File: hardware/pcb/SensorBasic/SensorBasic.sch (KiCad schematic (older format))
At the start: 4 parts

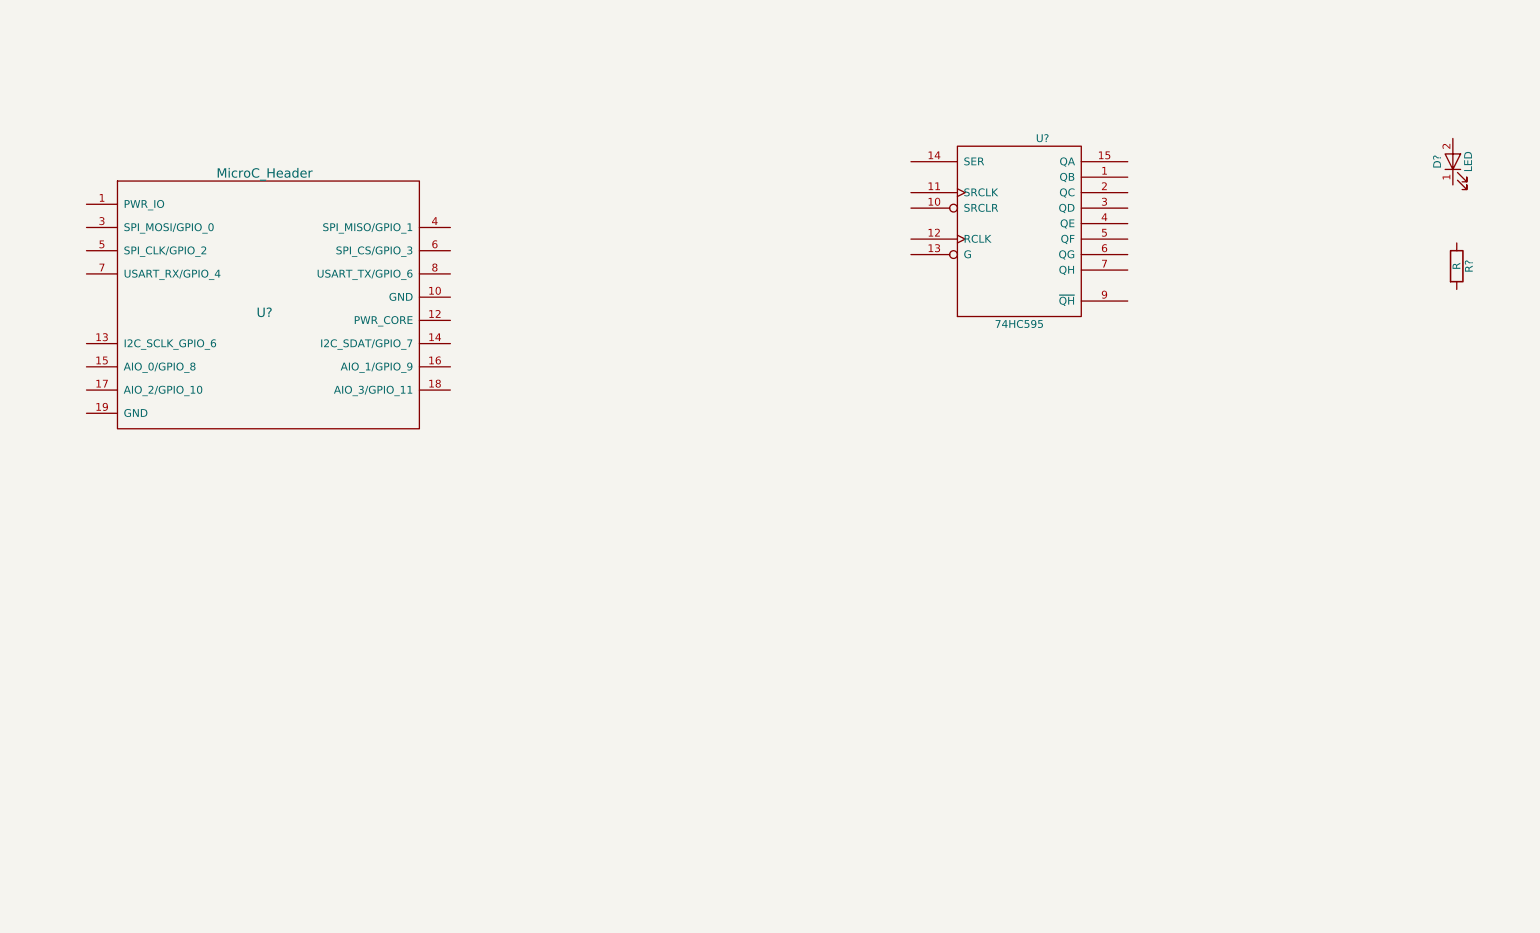
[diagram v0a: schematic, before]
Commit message: Initial schematic for Sensor
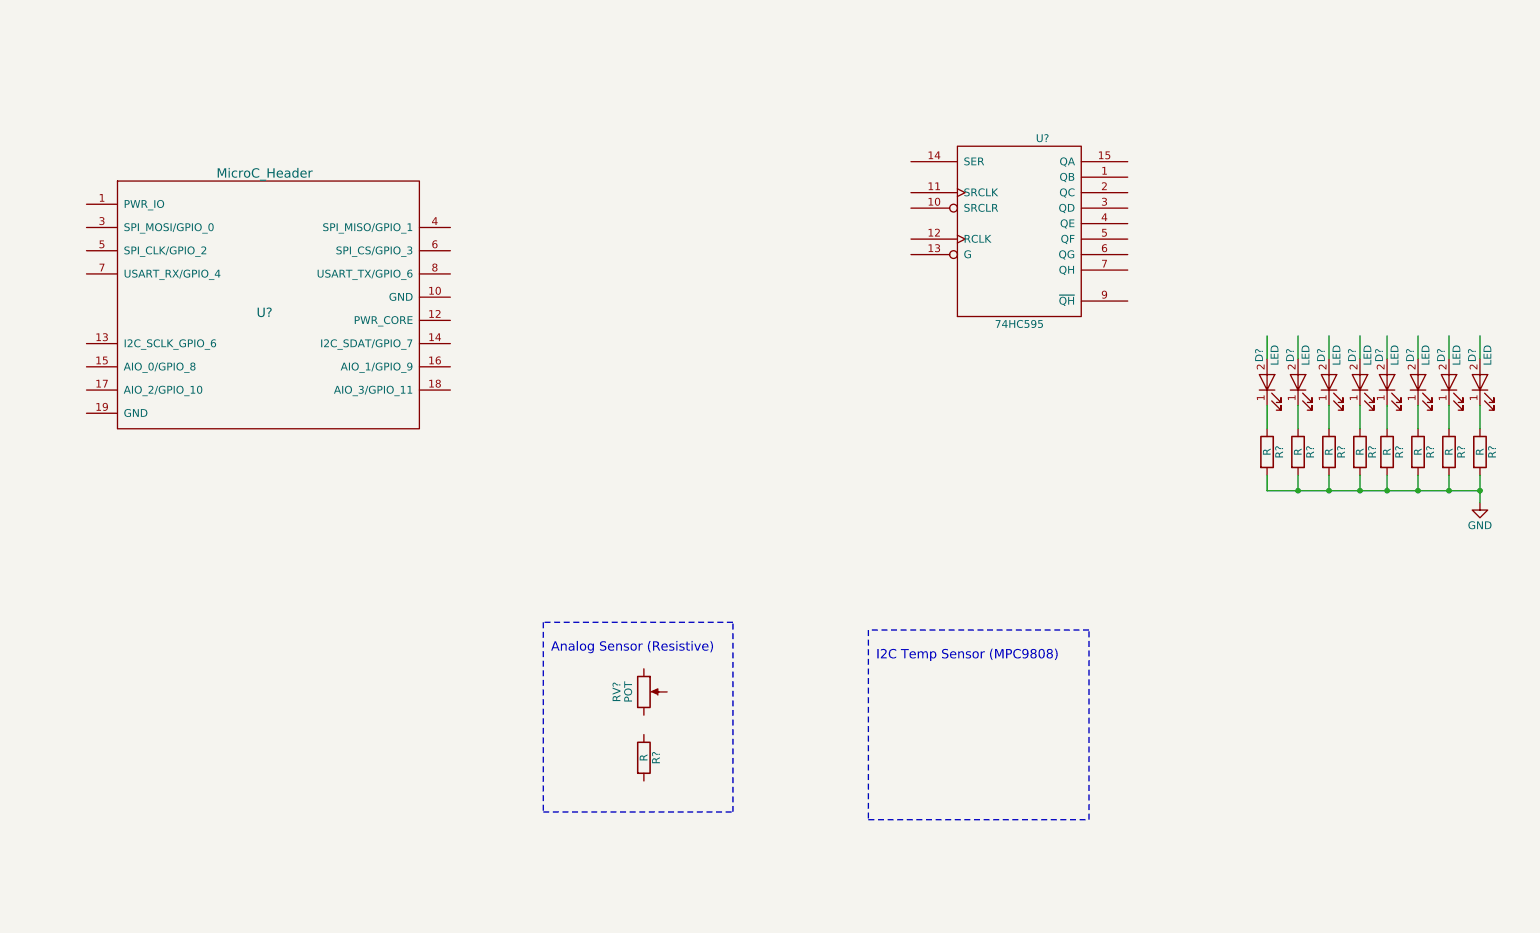
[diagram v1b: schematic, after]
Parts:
- added D? (x7): LED, symbol LED
- added R? (x8): R, symbol R
- added RV?: POT, symbol POT
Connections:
- net labels added: GND
- wire segments 0 -> 32
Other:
- note added: "Analog Sensor (Resistive)"
- note added: "I2C Temp Sensor (MPC9808)"
- moved on the sheet: D?, R?

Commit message: Add schematics symbol for temperature sensor, DS7505
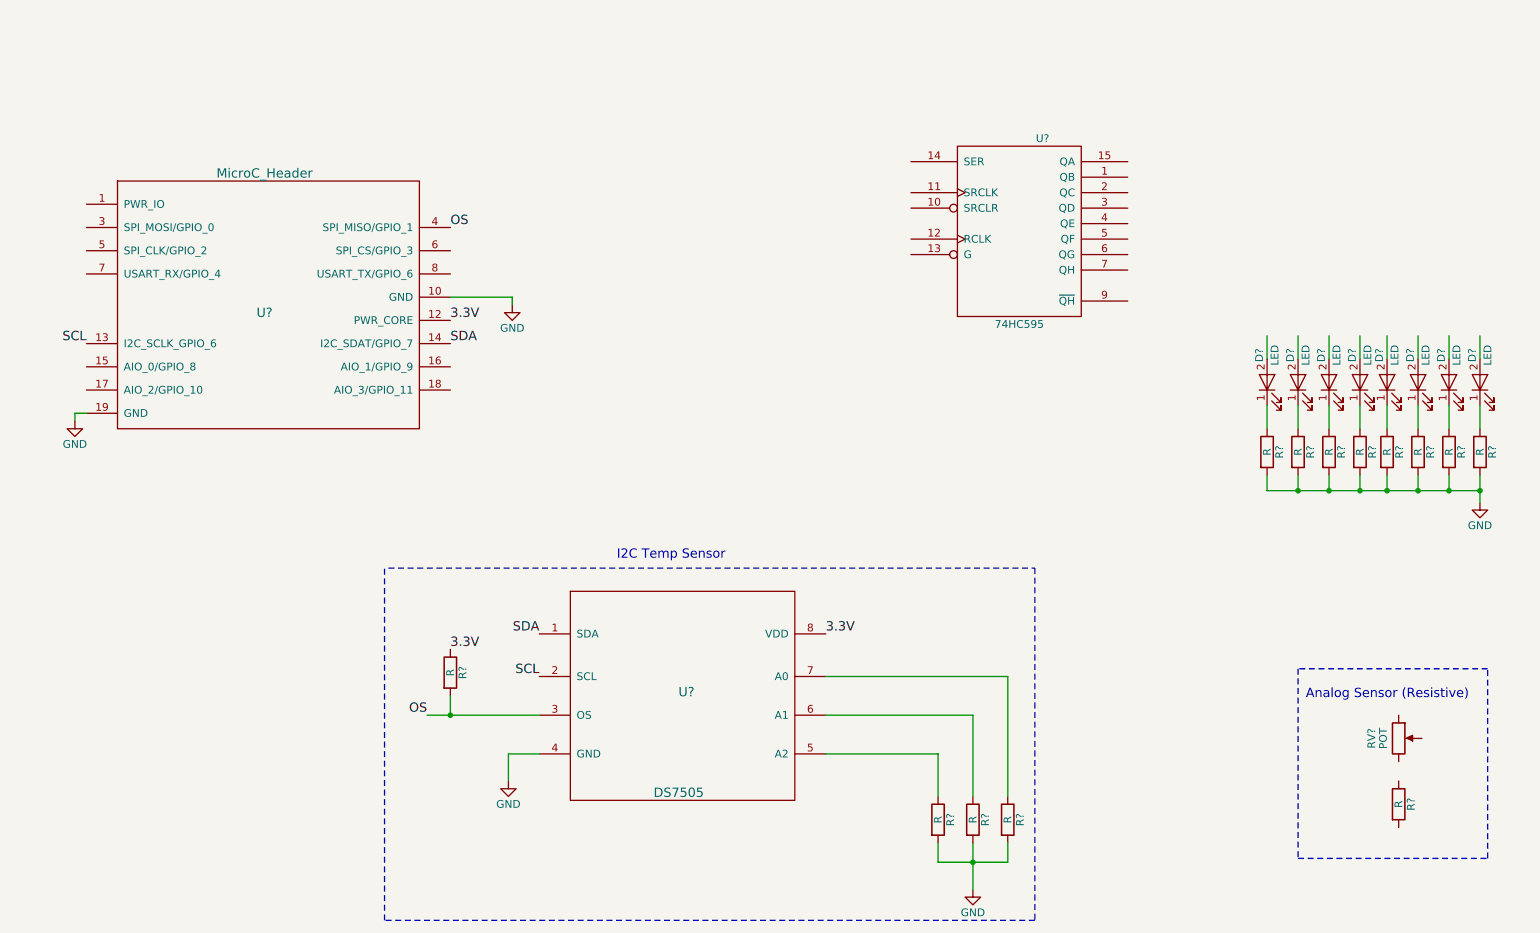
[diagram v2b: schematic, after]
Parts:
- added R? (x4): R, symbol R
- added U?: DS7505, symbol DS7505
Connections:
- net labels added: 3.3V, OS, SCL, SDA
- wire segments 32 -> 43
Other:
- note added: "I2C Temp Sensor"
- note removed: "I2C Temp Sensor (MPC9808)"
- moved on the sheet: R?, RV?
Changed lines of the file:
@@
 LIBS:valves
 LIBS:micro_c_header
+LIBS:SensorBasic
 LIBS:SensorBasic-cache
 EELAYER 25 0
@@
 	10425 2975 10425 3125
 Wire Wire Line
-	10425 3425 10425 3525
-Wire Wire Line
-	10425 3525 10425 3600
+	10425 3425 10425 3600
 Wire Wire Line
 	10425 2675 10425 2525
@@
 	9050 3425 9050 3525
 Wire Wire Line
-	9050 3525 9250 3525
-Wire Wire Line
-	9250 3525 9450 3525
-Wire Wire Line
-	9450 3525 9650 3525
-Wire Wire Line
-	9650 3525 9825 3525
-Wire Wire Line
-	9825 3525 10025 3525
-Wire Wire Line
-	10025 3525 10225 3525
-Wire Wire Line
-	10225 3525 10425 3525
+	9050 3525 10425 3525
 Connection ~ 10425 3525
 Wire Wire Line
@@
 L POT RV?
 U 1 1 593C8778
-P 5025 4825
-F 0 "RV?" V 4850 4825 50  0000 C CNN
-F 1 "POT" V 4925 4825 50  0000 C CNN
-F 2 "" H 5025 4825 50  0001 C CNN
-F 3 "" H 5025 4825 50  0001 C CNN
-	1    5025 4825
+P 9900 5125
+F 0 "RV?" V 9725 5125 50  0000 C CNN
+F 1 "POT" V 9800 5125 50  0000 C CNN
+F 2 "" H 9900 5125 50  0001 C CNN
+F 3 "" H 9900 5125 50  0001 C CNN
+	1    9900 5125
 	1    0    0    -1
 $EndComp
@@
 L R R?
 U 1 1 593C87E3
-P 5025 5250
-F 0 "R?" V 5105 5250 50  0000 C CNN
-F 1 "R" V 5025 5250 50  0000 C CNN
-F 2 "" V 4955 5250 50  0001 C CNN
-F 3 "" H 5025 5250 50  0001 C CNN
-	1    5025 5250
-	1    0    0    -1
-$EndComp
-Wire Notes Line
-	4375 4375 4375 5600
-Wire Notes Line
-	4375 5600 5600 5600
-Wire Notes Line
-	5600 5600 5600 4375
-Wire Notes Line
-	5600 4375 4375 4375
-Text Notes 4425 4575 0    60   ~ 0
+P 9900 5550
+F 0 "R?" V 9980 5550 50  0000 C CNN
+F 1 "R" V 9900 5550 50  0000 C CNN
+F 2 "" V 9830 5550 50  0001 C CNN
+F 3 "" H 9900 5550 50  0001 C CNN
+	1    9900 5550
+	1    0    0    -1
+$EndComp
+Wire Notes Line
+	9250 4675 9250 5900
+Wire Notes Line
+	9250 5900 10475 5900
+Wire Notes Line
+	10475 5900 10475 4675
+Wire Notes Line
+	10475 4675 9250 4675
+Text Notes 9300 4875 0    60   ~ 0
 Analog Sensor (Resistive)
-Wire Notes Line
-	6475 4425 6475 5650
-Wire Notes Line
-	6475 5650 7900 5650
-Wire Notes Line
-	7900 5650 7900 4425
-Wire Notes Line
-	7900 4425 6475 4425
-Text Notes 6525 4625 0    60   ~ 0
-I2C Temp Sensor (MPC9808)
+Text Notes 4850 3975 0    60   ~ 0
+I2C Temp Sensor
+$Comp
+L DS7505 U?
+U 1 1 593C8DEB
+P 5275 4825
+F 0 "U?" H 5300 4825 60  0000 C CNN
+F 1 "DS7505" H 5250 4175 60  0000 C CNN
+F 2 "" H 5275 4825 60  0001 C CNN
+F 3 "" H 5275 4825 60  0001 C CNN
+	1    5275 4825
+	1    0    0    -1
+$EndComp
+Text Label 4350 4450 2    60   ~ 0
+SDA
+Text Label 4350 4725 2    60   ~ 0
+SCL
+Text Label 6200 4450 0    60   ~ 0
+3.3V
+$Comp
+L R R?
+U 1 1 593C9210
+P 7375 5650
+F 0 "R?" V 7455 5650 50  0000 C CNN
+F 1 "R" V 7375 5650 50  0000 C CNN
+F 2 "" V 7305 5650 50  0001 C CNN
+F 3 "" H 7375 5650 50  0001 C CNN
+	1    7375 5650
+	1    0    0    -1
+$EndComp
+$Comp
+L R R?
+U 1 1 593C93DD
+P 7150 5650
+F 0 "R?" V 7230 5650 50  0000 C CNN
+F 1 "R" V 7150 5650 50  0000 C CNN
+F 2 "" V 7080 5650 50  0001 C CNN
+F 3 "" H 7150 5650 50  0001 C CNN
+	1    7150 5650
+	1    0    0    -1
+$EndComp
+$Comp
+L R R?
+U 1 1 593C9440
+P 6925 5650
+F 0 "R?" V 7005 5650 50  0000 C CNN
+F 1 "R" V 6925 5650 50  0000 C CNN
+F 2 "" V 6855 5650 50  0001 C CNN
+F 3 "" H 6925 5650 50  0001 C CNN
+	1    6925 5650
+	1    0    0    -1
+$EndComp
+Wire Wire Line
+	6925 5500 6925 5225
+Wire Wire Line
+	6925 5225 6200 5225
+Wire Wire Line
+	7150 5500 7150 4975
+Wire Wire Line
+	7150 4975 6200 4975
+Wire Wire Line
+	7375 5500 7375 4725
+Wire Wire Line
+	7375 4725 6200 4725
+Wire Wire Line
+	6925 5800 6925 5925
+Wire Wire Line
+	6925 5925 7375 5925
+Wire Wire Line
+	7375 5925 7375 5800
+Wire Wire Line
+	7150 5800 7150 6100
+Connection ~ 7150 5925
+$Comp
+L GND #PWR?
+U 1 1 593C984A
+P 1350 3075
+F 0 "#PWR?" H 1350 2825 50  0001 C CNN
+F 1 "GND" H 1350 2925 50  0000 C CNN
+F 2 "" H 1350 3075 50  0001 C CNN
+F 3 "" H 1350 3075 50  0001 C CNN
+	1    1350 3075
+	1    0    0    -1
+$EndComp
+Wire Wire Line
+	1350 3075 1350 3025
+Wire Wire Line
+	1350 3025 1425 3025
+$Comp
+L GND #PWR?
+U 1 1 593C9AB8
+P 7150 6100
+F 0 "#PWR?" H 7150 5850 50  0001 C CNN
+F 1 "GND" H 7150 5950 50  0000 C CNN
+F 2 "" H 7150 6100 50  0001 C CNN
+F 3 "" H 7150 6100 50  0001 C CNN
+	1    7150 6100
+	1    0    0    -1
+$EndComp
+Text Label 3775 2425 0    60   ~ 0
+3.3V
+$Comp
+L GND #PWR?
+U 1 1 593C9E5D
+P 4150 5400
+F 0 "#PWR?" H 4150 5150 50  0001 C CNN
+F 1 "GND" H 4150 5250 50  0000 C CNN
+F 2 "" H 4150 5400 50  0001 C CNN
+F 3 "" H 4150 5400 50  0001 C CNN
+	1    4150 5400
+	1    0    0    -1
+$EndComp
+Wire Wire Line
+	4150 5400 4150 5225
+Wire Wire Line
+	4150 5225 4350 5225
+$Comp
+L GND #PWR?
+U 1 1 593C9FEB
+P 4175 2325
+F 0 "#PWR?" H 4175 2075 50  0001 C CNN
+F 1 "GND" H 4175 2175 50  0000 C CNN
+F 2 "" H 4175 2325 50  0001 C CNN
+F 3 "" H 4175 2325 50  0001 C CNN
+	1    4175 2325
+	1    0    0    -1
+$EndComp
+Wire Wire Line
+	3775 2275 4175 2275
+Wire Wire Line
+	4175 2275 4175 2325
+Text Label 3625 4975 2    60   ~ 0
+OS
+Text Label 3775 1825 0    60   ~ 0
+OS
+Wire Wire Line
+	4350 4975 3625 4975
+$Comp
+L R R?
+U 1 1 593CA7AD
+P 3775 4700
+F 0 "R?" V 3855 4700 50  0000 C CNN
+F 1 "R" V 3775 4700 50  0000 C CNN
+F 2 "" V 3705 4700 50  0001 C CNN
+F 3 "" H 3775 4700 50  0001 C CNN
+	1    3775 4700
+	1    0    0    -1
+$EndComp
+Wire Wire Line
+	3775 4850 3775 4975
+Connection ~ 3775 4975
+Text Label 3775 4550 0    60   ~ 0
+3.3V
+Wire Notes Line
+	3375 4025 7550 4025
+Wire Notes Line
+	7550 4025 7550 6300
+Wire Notes Line
+	7550 6300 3350 6300
+Wire Notes Line
+	3350 6300 3350 4025
+Text Label 3775 2575 0    60   ~ 0
+SDA
+Text Label 1425 2575 2    60   ~ 0
+SCL
 $EndSCHEMATC

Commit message: Final schematic
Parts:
- removed RV?: POT, symbol POT
- removed U?: 74HC595, symbol 74HC595
- added C? (x3): C, symbol C
- added R?: Photo Resistor, symbol R_PHOTO
- added R?: R, symbol R
- added U?: 74HC595-PWR, symbol 74HC595-PWR
- U?: MPN (none) -> DS7505S+T&R
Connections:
- net labels added: 5V, PR_BOT, PR_TOP, clockPin, dataPin, latchPin
- wire segments 43 -> 71
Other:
- moved on the sheet: R?

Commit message: Add footprint association and initial layout
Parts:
- C1, C2, C3: renamed from C?; footprint (none) -> Capacitors_SMD:C_0805_HandSoldering
- D1, D2, D3, D4, D5, D6, D7, D8: renamed from D?; footprint (none) -> LEDs:LED_0805
- R1, R10, R12, R13, R14, R15, R2, R3, R4, R5, R6, R7, R8, R9: renamed from R?; footprint (none) -> Resistors_SMD:R_0805_HandSoldering
- R11: renamed from R?; footprint (none) -> Capacitors_ThroughHole:CP_Radial_Tantal_D5.5mm_P5.00mm
- U1: renamed from U?; footprint (none) -> micro_c_header:MicroC_Header_Pitch2.54mm
- U2: renamed from U?; footprint (none) -> Housings_SOIC:SOIC-8_3.9x4.9mm_Pitch1.27mm
- U3: renamed from U?; footprint (none) -> Housings_SOIC:SOIC-16_3.9x9.9mm_Pitch1.27mm

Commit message: Added MPN part numbers to all parts except the resistors
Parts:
- C1, C2, C3: value C -> .1; MPN (none) -> C0805C104K5RACTU
- D1, D2, D3, D4, D5, D6, D7, D8: MPN (none) -> SML-LXR85IC-TR
- U2: MPN DS7505S+T&R -> DS7505S+-ND
- U3: MPN (none) -> 74HC595D,118
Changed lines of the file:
@@
 F 1 "LED" H 10600 2775 50  0000 C CNN
 F 2 "LEDs:LED_0805" H 10425 2825 50  0001 C CNN
-F 3 "" H 10425 2825 50  0001 C CNN
+F 3 "http://www.lumex.com/content/files/ProductAttachment/SML-LXR85IC-TR.pdf" H 10425 2825 50  0001 C CNN
+F 4 "SML-LXR85IC-TR" H 10425 2825 60  0001 C CNN "MPN"
 	1    10425 2825
 	0    -1   -1   0
@@
 F 1 "LED" H 10400 2775 50  0000 C CNN
 F 2 "LEDs:LED_0805" H 10225 2825 50  0001 C CNN
-F 3 "" H 10225 2825 50  0001 C CNN
+F 3 "http://www.lumex.com/content/files/ProductAttachment/SML-LXR85IC-TR.pdf" H 10225 2825 50  0001 C CNN
+F 4 "SML-LXR85IC-TR" H 10225 2825 60  0001 C CNN "MPN"
 	1    10225 2825
 	0    -1   -1   0
@@
 F 1 "LED" H 10200 2775 50  0000 C CNN
 F 2 "LEDs:LED_0805" H 10025 2825 50  0001 C CNN
-F 3 "" H 10025 2825 50  0001 C CNN
+F 3 "http://www.lumex.com/content/files/ProductAttachment/SML-LXR85IC-TR.pdf" H 10025 2825 50  0001 C CNN
+F 4 "SML-LXR85IC-TR" H 10025 2825 60  0001 C CNN "MPN"
 	1    10025 2825
 	0    -1   -1   0
@@
 F 1 "LED" H 10000 2775 50  0000 C CNN
 F 2 "LEDs:LED_0805" H 9825 2825 50  0001 C CNN
-F 3 "" H 9825 2825 50  0001 C CNN
+F 3 "http://www.lumex.com/content/files/ProductAttachment/SML-LXR85IC-TR.pdf" H 9825 2825 50  0001 C CNN
+F 4 "SML-LXR85IC-TR" H 9825 2825 60  0001 C CNN "MPN"
 	1    9825 2825
 	0    -1   -1   0
@@
 F 1 "LED" H 9825 2775 50  0000 C CNN
 F 2 "LEDs:LED_0805" H 9650 2825 50  0001 C CNN
-F 3 "" H 9650 2825 50  0001 C CNN
+F 3 "http://www.lumex.com/content/files/ProductAttachment/SML-LXR85IC-TR.pdf" H 9650 2825 50  0001 C CNN
+F 4 "SML-LXR85IC-TR" H 9650 2825 60  0001 C CNN "MPN"
 	1    9650 2825
 	0    -1   -1   0
@@
 F 1 "LED" H 9625 2775 50  0000 C CNN
 F 2 "LEDs:LED_0805" H 9450 2825 50  0001 C CNN
-F 3 "" H 9450 2825 50  0001 C CNN
+F 3 "http://www.lumex.com/content/files/ProductAttachment/SML-LXR85IC-TR.pdf" H 9450 2825 50  0001 C CNN
+F 4 "SML-LXR85IC-TR" H 9450 2825 60  0001 C CNN "MPN"
 	1    9450 2825
 	0    -1   -1   0
@@
 F 1 "LED" H 9425 2775 50  0000 C CNN
 F 2 "LEDs:LED_0805" H 9250 2825 50  0001 C CNN
-F 3 "" H 9250 2825 50  0001 C CNN
+F 3 "http://www.lumex.com/content/files/ProductAttachment/SML-LXR85IC-TR.pdf" H 9250 2825 50  0001 C CNN
+F 4 "SML-LXR85IC-TR" H 9250 2825 60  0001 C CNN "MPN"
 	1    9250 2825
 	0    -1   -1   0
@@
 F 1 "LED" H 9225 2775 50  0000 C CNN
 F 2 "LEDs:LED_0805" H 9050 2825 50  0001 C CNN
-F 3 "" H 9050 2825 50  0001 C CNN
+F 3 "http://www.lumex.com/content/files/ProductAttachment/SML-LXR85IC-TR.pdf" H 9050 2825 50  0001 C CNN
+F 4 "SML-LXR85IC-TR" H 9050 2825 60  0001 C CNN "MPN"
 	1    9050 2825
 	0    -1   -1   0
@@
 F 2 "Housings_SOIC:SOIC-8_3.9x4.9mm_Pitch1.27mm" H 5275 4825 60  0001 C CNN
 F 3 "https://datasheets.maximintegrated.com/en/ds/DS7505.pdf" H 5275 4825 60  0001 C CNN
-F 4 "DS7505S+T&R" H 5275 4825 60  0001 C CNN "MPN"
+F 4 "DS7505S+-ND" H 5275 4825 60  0001 C CNN "MPN"
 	1    5275 4825
 	1    0    0    -1
@@
 F 1 "74HC595-PWR" H 6850 1150 50  0000 C CNN
 F 2 "Housings_SOIC:SOIC-16_3.9x9.9mm_Pitch1.27mm" H 6850 1750 50  0001 C CNN
-F 3 "" H 6850 1750 50  0001 C CNN
+F 3 "https://assets.nexperia.com/documents/data-sheet/74HC_HCT595.pdf" H 6850 1750 50  0001 C CNN
+F 4 "74HC595D,118" H 6850 1750 60  0001 C CNN "MPN"
 	1    6850 1750
 	1    0    0    -1
@@
 P 5750 2150
 F 0 "C1" H 5775 2250 50  0000 L CNN
-F 1 "C" H 5775 2050 50  0000 L CNN
+F 1 ".1" H 5775 2050 50  0000 L CNN
 F 2 "Capacitors_SMD:C_0805_HandSoldering" H 5788 2000 50  0001 C CNN
-F 3 "" H 5750 2150 50  0001 C CNN
+F 3 "http://www.kemet.com/docfinder?Partnumber=C0805C104K5RACTU" H 5750 2150 50  0001 C CNN
+F 4 "C0805C104K5RACTU" H 5750 2150 60  0001 C CNN "MPN"
 	1    5750 2150
 	1    0    0    -1
@@
 P 7400 1025
 F 0 "C3" H 7425 1125 50  0000 L CNN
-F 1 "C" H 7425 925 50  0000 L CNN
+F 1 ".1" H 7425 925 50  0000 L CNN
 F 2 "Capacitors_SMD:C_0805_HandSoldering" H 7438 875 50  0001 C CNN
-F 3 "" H 7400 1025 50  0001 C CNN
+F 3 "http://www.kemet.com/docfinder?Partnumber=C0805C104K5RACTU" H 7400 1025 50  0001 C CNN
+F 4 "C0805C104K5RACTU" H 7400 1025 60  0001 C CNN "MPN"
 	1    7400 1025
 	0    1    1    0
@@
 P 6725 4450
 F 0 "C2" H 6750 4550 50  0000 L CNN
-F 1 "C" H 6750 4350 50  0000 L CNN
+F 1 ".1" H 6750 4350 50  0000 L CNN
 F 2 "Capacitors_SMD:C_0805_HandSoldering" H 6763 4300 50  0001 C CNN
-F 3 "" H 6725 4450 50  0001 C CNN
+F 3 "http://www.kemet.com/docfinder?Partnumber=C0805C104K5RACTU" H 6725 4450 50  0001 C CNN
+F 4 "C0805C104K5RACTU" H 6725 4450 60  0001 C CNN "MPN"
 	1    6725 4450
 	0    1    1    0
